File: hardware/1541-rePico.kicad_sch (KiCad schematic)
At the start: 14 parts, among them J1 Display Connector, J2 Display Power, J3 Conn_01x05_Pin, J4 SD Card Module Connector, J5 Conn_01x01_Pin, J6 EXT_5V, J7 RESET_1541, SW1 RESET, U1 Pico

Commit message: modified PCB for Sound-connector
updated PCB to version 1.7
changes include:
- removal of SW-DBG header
- addition of Buzzer-connector
- changed layout of display-connector (straight vs. square)
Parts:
- removed SWDBG1: DEBUG, Connector_PinHeader_2.54mm:PinHeader_1x03_P2.54mm_Vertical, symbol Connector_Generic:Conn_01x03
- added BZ1: Buzzer, Buzzer_Beeper:Buzzer_TDK_PS1240P02BT_D12.2mm_H6.5mm, symbol Device:Buzzer
- added J8: Buzzer Connector, Connector_PinSocket_2.54mm:PinSocket_1x02_P2.54mm_Vertical, symbol Connector_Generic:Conn_01x02
- J1: footprint Connector_PinSocket_2.54mm:PinSocket_2x02_P2.54mm_Vertical -> Connector_PinSocket_2.54mm:PinSocket_1x04_P2.54mm_Vertical; symbol Connector_Generic:Conn_02x02_Odd_Even -> Connector_Generic:Conn_01x04
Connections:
- net GND: now also J1.1 (Pin_1), J4.10 (Pin_10), J4.9 (Pin_9), BZ1.2 (-), J8.1 (Pin_1); no longer J1.2 (Pin_2)
- net at J2.2 (Pin_2): now also J1.2 (Pin_2); no longer J1.1 (Pin_1)
- removed net CS: J4.10 (Pin_10), J4.9 (Pin_9), U1.22 (GPIO17)
- new net BUZZER+: BZ1.1 (+), J8.2 (Pin_2), U1.22 (GPIO17)
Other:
- moved on the sheet: J1, R1, R2

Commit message: PCB 1.7 fixes and files
updated PCB 1.7 layout:
- rotated SDCard connector
- placed silkscreen text for orientation
- added buzzer-footprint
updated pdf for SCH and PCB files
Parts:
- J5: footprint Connector_PinHeader_2.00mm:PinHeader_1x01_P2.00mm_Vertical -> Connector_PinHeader_2.54mm:PinHeader_1x01_P2.54mm_Vertical
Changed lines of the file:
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@@
 	(title_block
 		(title "1541-rePico")
-		(date "2026-08-02")
+		(date "2026-08-06")
 		(rev "1.7")
 	)
@@
 		(exclude_from_sim no)
 		(in_bom yes)
-		(on_board no)
+		(on_board yes)
 		(dnp no)
 		(fields_autoplaced yes)
@@
 			)
 		)
-		(property "Footprint" "Connector_PinHeader_2.00mm:PinHeader_1x01_P2.00mm_Vertical"
+		(property "Footprint" "Connector_PinHeader_2.54mm:PinHeader_1x01_P2.54mm_Vertical"
 			(at 168.91 87.63 0)
 			(effects

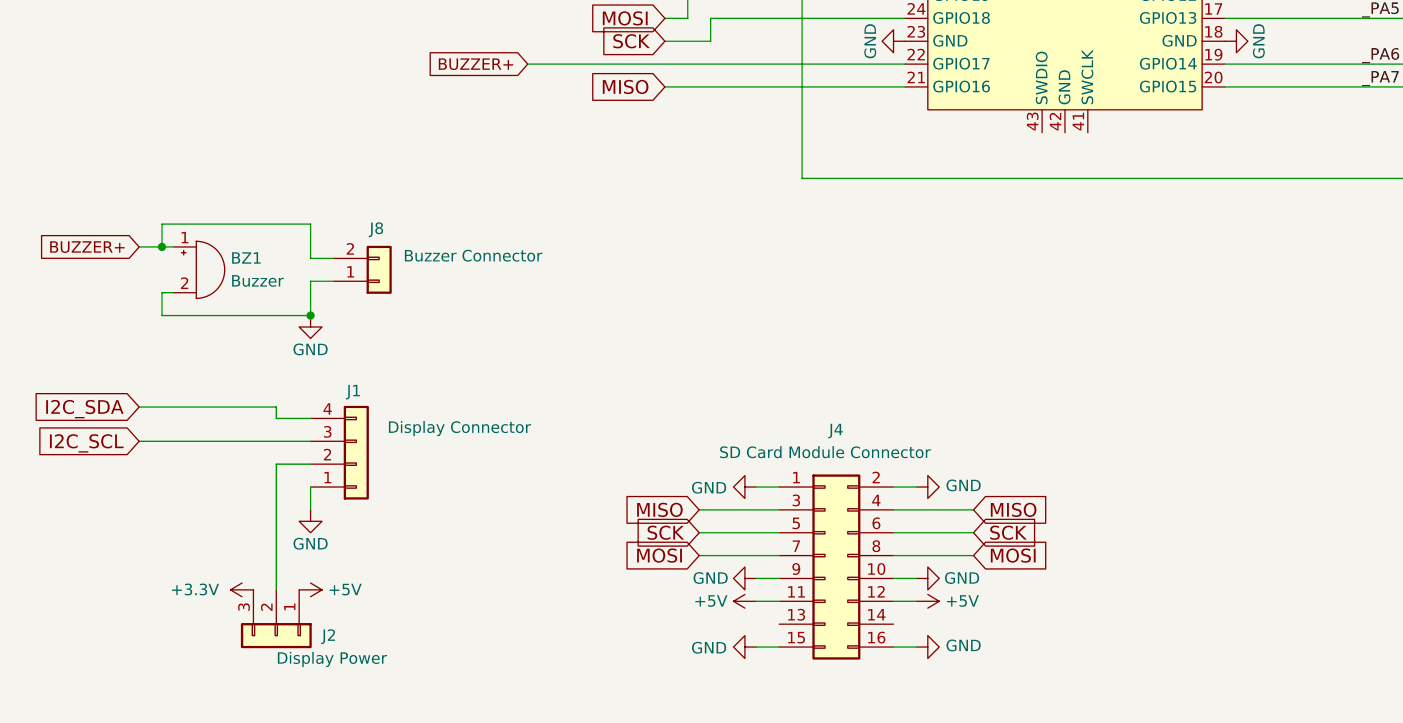
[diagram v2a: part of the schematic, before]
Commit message: update PCB to V1.7.0
added jumper-selector for SD-Card VCC (3.3V vs 5V)
slight movements of Buzzer, SDCard-header
changed Footprint of Buzzer to fit passive Buzzer-pin distance
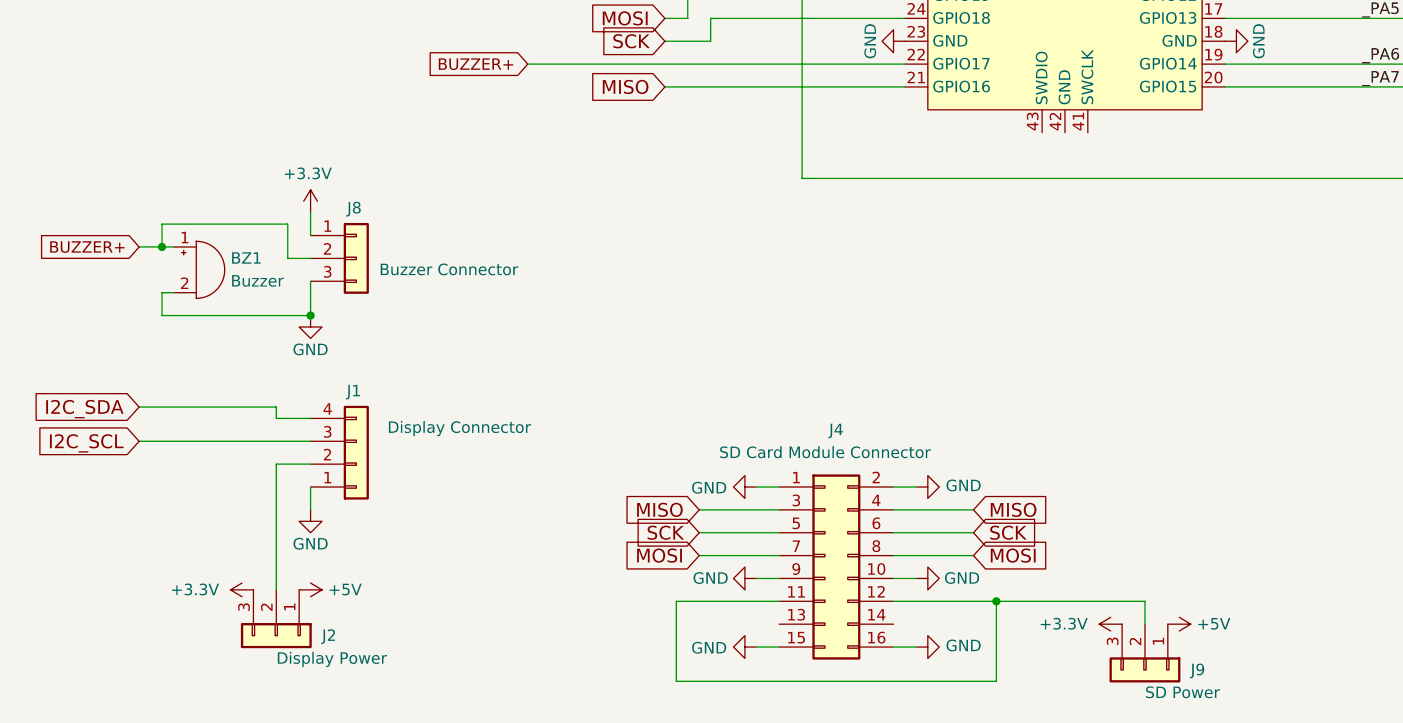
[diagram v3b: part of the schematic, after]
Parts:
- removed J8: Buzzer Connector, Connector_PinSocket_2.54mm:PinSocket_1x02_P2.54mm_Vertical, symbol Connector_Generic:Conn_01x02
- added J8: Buzzer Connector, Connector_PinHeader_2.54mm:PinHeader_1x03_P2.54mm_Vertical, symbol Connector_Generic:Conn_01x03
- added J9: SD Power, Connector_PinHeader_2.54mm:PinHeader_1x03_P2.54mm_Vertical, symbol Connector_Generic:Conn_01x03
- BZ1: footprint Buzzer_Beeper:Buzzer_TDK_PS1240P02BT_D12.2mm_H6.5mm -> Buzzer_Beeper:MagneticBuzzer_StarMicronics_QMX
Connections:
- net +3.3V: now also J8.1 (Pin_1), J9.3 (Pin_3)
- net +5V: now also J9.1 (Pin_1); no longer J4.11 (Pin_11), J4.12 (Pin_12)
- net BUZZER+: now also J8.2 (Pin_2)
- net GND: now also J8.3 (Pin_3)
- new net: J4.11 (Pin_11), J4.12 (Pin_12), J9.2 (Pin_2)
